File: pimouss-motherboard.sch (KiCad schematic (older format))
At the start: 0 parts

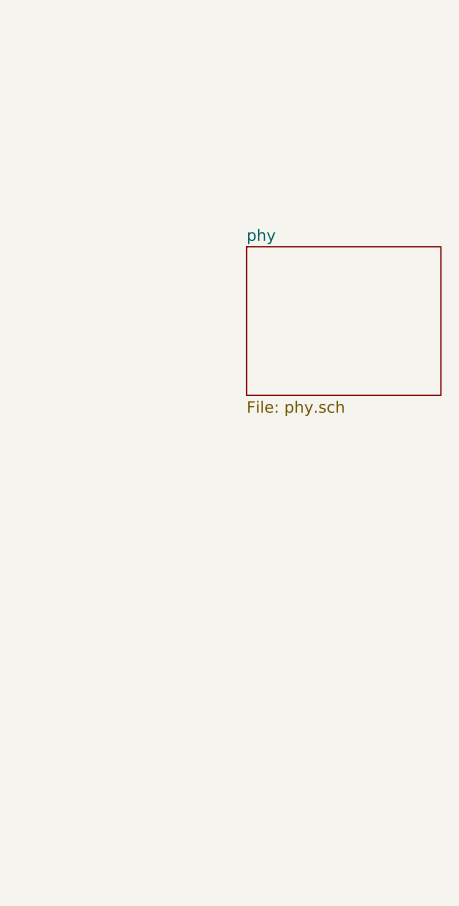
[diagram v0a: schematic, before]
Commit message: sch: USB-Serial console done
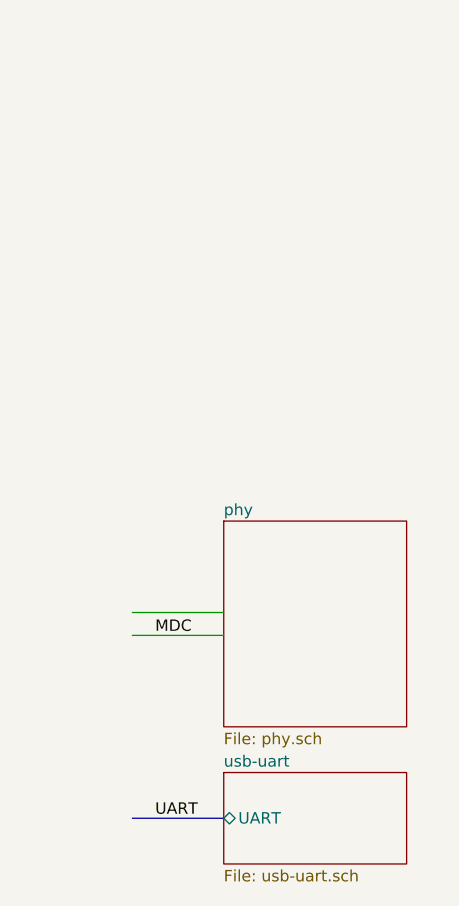
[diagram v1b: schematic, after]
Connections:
- net labels added: MDC, UART
- wire segments 0 -> 2
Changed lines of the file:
@@
 EESchema Schematic File Version 4
+LIBS:pimouss-motherboard-cache
 EELAYER 26 0
 EELAYER END
@@
 $EndDescr
 $Sheet
-S 4800 2600 850  650
+S 4700 3800 800  900
 U 5C7D0D1E
 F0 "phy" 50
 F1 "phy.sch" 50
 $EndSheet
+$Sheet
+S 4700 4900 800  400
+U 5D2774DB
+F0 "usb-uart" 50
+F1 "usb-uart.sch" 50
+F2 "UART" B L 4700 5100 50
+$EndSheet
+Wire Bus Line
+	4700 5100 4300 5100
+Text Label 4400 5100 0    50   ~ 0
+UART
+Text Label 4400 4300 0    50   ~ 0
+MDC
+Wire Wire Line
+	4300 4300 4700 4300
+Wire Wire Line
+	4300 4200 4700 4200
 $EndSCHEMATC

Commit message: sch: Pimouss connector done
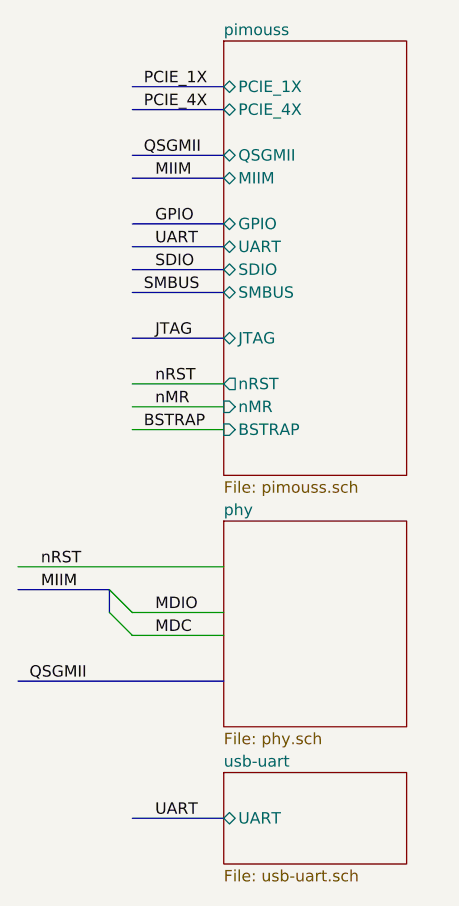
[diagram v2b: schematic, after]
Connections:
- net labels added: BSTRAP, GPIO, JTAG, MDIO, MIIM, PCIE_1X, PCIE_4X, QSGMII, SDIO, SMBUS, nMR, nRST
- wire segments 2 -> 6
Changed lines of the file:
@@
 $EndSheet
+$Sheet
+S 4700 1700 800  1900
+U 5CE77C37
+F0 "pimouss" 50
+F1 "pimouss.sch" 50
+F2 "PCIE_1X" B L 4700 1900 50
+F3 "PCIE_4X" B L 4700 2000 50
+F4 "QSGMII" B L 4700 2200 50
+F5 "MIIM" B L 4700 2300 50
+F6 "GPIO" B L 4700 2500 50
+F7 "UART" B L 4700 2600 50
+F8 "SDIO" B L 4700 2700 50
+F9 "SMBUS" B L 4700 2800 50
+F10 "JTAG" B L 4700 3000 50
+F11 "nRST" O L 4700 3200 50
+F12 "nMR" I L 4700 3300 50
+F13 "BSTRAP" I L 4700 3400 50
+$EndSheet
+Wire Bus Line
+	4700 1900 4300 1900
+Text Label 4350 1900 0    50   ~ 0
+PCIE_1X
+Wire Bus Line
+	4700 2000 4300 2000
+Text Label 4350 2000 0    50   ~ 0
+PCIE_4X
+Wire Bus Line
+	4700 2200 4300 2200
+Text Label 4350 2200 0    50   ~ 0
+QSGMII
+Wire Bus Line
+	4300 2300 4700 2300
+Text Label 4400 2300 0    50   ~ 0
+MIIM
+Wire Bus Line
+	4700 2500 4300 2500
+Text Label 4400 2500 0    50   ~ 0
+GPIO
+Wire Bus Line
+	4700 2600 4300 2600
+Text Label 4400 2600 0    50   ~ 0
+UART
+Wire Bus Line
+	4700 2700 4300 2700
+Text Label 4400 2700 0    50   ~ 0
+SDIO
+Wire Bus Line
+	4700 2800 4300 2800
+Text Label 4350 2800 0    50   ~ 0
+SMBUS
+Wire Bus Line
+	4700 3000 4300 3000
+Text Label 4400 3000 0    50   ~ 0
+JTAG
+Wire Wire Line
+	4300 3200 4700 3200
+Wire Wire Line
+	4300 3300 4700 3300
+Text Label 4400 3200 0    50   ~ 0
+nRST
+Text Label 4400 3300 0    50   ~ 0
+nMR
+Wire Wire Line
+	4300 3400 4700 3400
+Text Label 4350 3400 0    50   ~ 0
+BSTRAP
+Wire Wire Line
+	3800 4000 4700 4000
+Text Label 3900 4000 0    50   ~ 0
+nRST
+Wire Bus Line
+	4700 4500 3800 4500
+Text Label 3850 4500 0    50   ~ 0
+QSGMII
+Text Label 4400 4200 0    50   ~ 0
+MDIO
+Wire Bus Line
+	4200 4200 4200 4100
+Entry Wire Line
+	4200 4200 4300 4300
+Entry Wire Line
+	4200 4100 4300 4200
+Wire Bus Line
+	3800 4100 4200 4100
+Text Label 3900 4100 0    50   ~ 0
+MIIM
 $Sheet
 S 4700 4900 800  400
